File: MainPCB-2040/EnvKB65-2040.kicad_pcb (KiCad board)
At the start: 2 copper layers, 320.8 x 99.7 mm, 203 parts, among them J2 SKRKAEE020, J5 Conn_01x03_Male, U1 TLV73333PDBV, U3 RP2040, Y1 Crystal

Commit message: continued work on the RP2040 version
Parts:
- C1, C10, C4, D1, R3, R4, R5, R6, R8, U1: moved to B.Cu
- FLASH1: footprint Package_SO:SOIJ-8_5.3x5.3mm_P1.27mm -> Package_SON:SON-8-1EP_3x2mm_P0.5mm_EP1.4x1.6mm; moved to B.Cu
- moved R4 32.3 mm to (344.3, 106.0), turned to 270 degrees
- moved R5 29.3 mm to (365.5, 106.3)
- moved R8 27.3 mm to (340.4, 111.2)
- moved C10 26.7 mm to (343.3, 106.7), turned to 90 degrees
- moved R6 25.6 mm to (370.1, 106.4), turned to 180 degrees
- moved R3 25.3 mm to (345.2, 106.0), turned to 270 degrees
- moved FLASH1 23.1 mm to (349.1, 106.2), turned to 180 degrees
- moved D1 18.9 mm to (352.9, 100.9)
- moved U1 18.2 mm to (348.7, 99.8), turned to 180 degrees
- moved C1 14.3 mm to (352.7, 98.9)
- moved D3 7.73 mm to (342.0, 98.8)
- moved C4 6.40 mm to (344.6, 98.8), turned to 180 degrees
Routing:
- net USB_D-: track 0.00 -> 34.9 mm, vias 0 -> 2
- net USB_D+: track 0.00 -> 30.9 mm, vias 0 -> 2
- net VBUS: track 0.00 -> 23.5 mm, vias 0 -> 2
- net +3V3: track 0.00 -> 19.6 mm, vias 0 -> 2
- net Net-(D3-Pad2): track 0.00 -> 15.4 mm, vias 0 -> 1
- net GND: track 0.00 -> 12.8 mm, vias 4 -> 8
- net +1V1: track 0.00 -> 9.59 mm, vias 0 -> 5
- net VSYS: track 0.00 -> 6.70 mm
- net /QSPI_SS: track 0.00 -> 6.22 mm
- net /QSPI_SD1: track 0.00 -> 6.01 mm
- net /QSPI_SD2: track 0.00 -> 5.44 mm
- net /QSPI_SD3: track 0.00 -> 3.18 mm
- net /QSPI_SCLK: track 0.00 -> 2.49 mm
- net Net-(R3-Pad2): track 0.00 -> 1.97 mm
- net Net-(R4-Pad2): track 0.00 -> 1.96 mm
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- added copper zone on B.Cu, net +1V1
- added copper zone on B.Cu, net +3V3
- added copper zone on B.Cu, net VBUS

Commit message: finished off RP2040 version, needs general check overs and cleanup.
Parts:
- removed C17: 10uf 0402, Capacitor_SMD:C_0402_1005Metric
- removed C18: 100nf 0402, Capacitor_SMD:C_0402_1005Metric
- removed TP1, TP2, TP3, TP4, TP5, TP6, TP7, TP8: TestPoint, TestPoint:TestPoint_Pad_D1.0mm
- added J1: SKRKAEE020, Button_Switch_SMD:SW_Push_SPST_NO_Alps_SKRK, F.Cu at (357.3, 99.7)
- C11, C13, C19, C2, C5, R2, Y1: moved to B.Cu
- J5: footprint Connector_PinHeader_2.54mm:PinHeader_1x03_P2.54mm_Vertical -> Connector_PinHeader_1.00mm:PinHeader_1x03_P1.00mm_Horizontal
- moved Y1 49.9 mm to (346.7, 120.0), turned to 180 degrees
- moved C11 43.8 mm to (345.7, 117.2), turned to 270 degrees
- moved C19 43.4 mm to (346.4, 122.2)
- moved C15 37.8 mm to (346.5, 114.3)
- moved C2 37.5 mm to (349.5, 120.8), turned to 270 degrees
- moved J5 34.5 mm to (337.1, 101.0), turned to 90 degrees
- moved R2 32.3 mm to (351.1, 109.0)
- moved C7 31.7 mm to (345.8, 116.1)
- moved C16 31.0 mm to (346.2, 104.1), turned to 90 degrees
- moved C8 30.4 mm to (347.8, 109.2), turned to 180 degrees
- moved C14 25.6 mm to (348.9, 112.8)
- moved C13 25.1 mm to (340.3, 112.5), turned to 180 degrees
- moved J2 24.7 mm to (349.9, 99.7)
- moved C3 23.2 mm to (345.9, 109.2)
- moved C5 17.7 mm to (346.6, 105.2), turned to 45 degrees
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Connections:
- U3 pad 11: (no net) -> row2
- U3 pad 12: (no net) -> row1
- U3 pad 13: (no net) -> row0
- U3 pad 14: (no net) -> col14
- U3 pad 15: (no net) -> col13
- U3 pad 16: (no net) -> col12
- U3 pad 17: (no net) -> col11
- U3 pad 18: (no net) -> col10
- U3 pad 2: (no net) -> col15
- U3 pad 26: (no net) -> /RUN
- U3 pad 27: (no net) -> col9
- U3 pad 28: (no net) -> col8
- U3 pad 29: (no net) -> col7
- U3 pad 3: (no net) -> col16
- U3 pad 30: (no net) -> col6
- U3 pad 31: (no net) -> col5
- U3 pad 32: (no net) -> col4
- U3 pad 34: (no net) -> col3
- U3 pad 38: (no net) -> col2
- U3 pad 39: (no net) -> col1
- U3 pad 40: (no net) -> col0
- U3 pad 8: (no net) -> row4
- U3 pad 9: (no net) -> row3
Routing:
- net /RUN: track 0.00 -> 48.0 mm, vias 0 -> 1
- net GND: track 12.8 -> 41.6 mm, vias 8 -> 21
- net col13: track 113.9 -> 137.0 mm, vias 1 -> 3
- net /SWCLK: track 0.00 -> 21.6 mm, vias 0 -> 2
- net /SWD: track 0.00 -> 19.4 mm, vias 0 -> 2
- net VBUS: track 23.5 -> 5.10 mm
- net col4: track 278.7 -> 295.5 mm
- net col3: track 303.0 -> 319.3 mm
- net col12: track 144.2 -> 159.7 mm
- net col0: track 362.8 -> 378.1 mm
- net col2: track 297.0 -> 312.1 mm
- net col1: track 328.0 -> 342.9 mm
- net col11: track 161.3 -> 174.9 mm
- net col10: track 182.7 -> 194.5 mm
- net XOUT: track 0.00 -> 8.01 mm
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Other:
- board text added: "BOOTSEL"
- board text added: "GND"
- board text added: "RESET"
- board text added: "SWCLK"
- board text added: "SWD"
- board text removed: "http://github.com/Envious-Data/Env-KB65M"

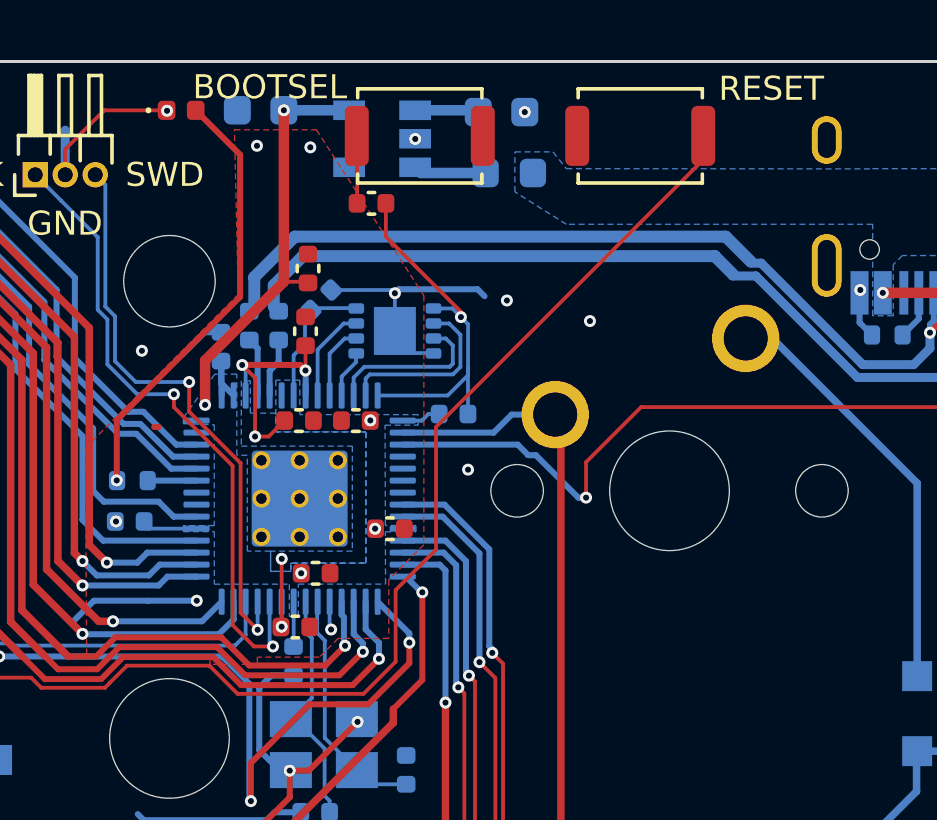
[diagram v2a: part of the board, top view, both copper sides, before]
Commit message: moved some resistors and capacitors to account for screw hole clearance for the stabilizer holes.
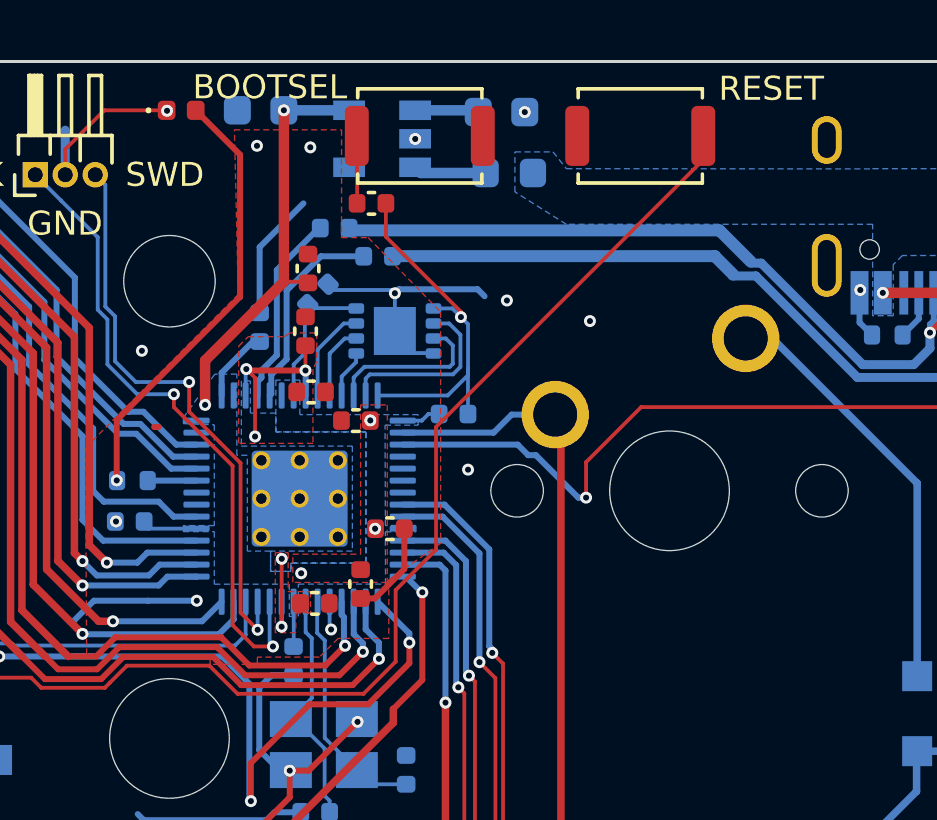
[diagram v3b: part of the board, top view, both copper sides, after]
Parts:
- moved R4 4.32 mm to (347.1, 102.8), turned to 180 degrees
- moved R3 4.04 mm to (348.5, 103.7), turned to 180 degrees
- moved C15 1.54 mm to (348.0, 114.6), turned to 270 degrees
- moved C10 1.44 mm to (344.6, 106.1)
- moved C3 1.04 mm to (346.3, 108.2)
- moved C7 1.02 mm to (346.4, 115.3)
- moved C5 0.22 mm to (346.5, 105.0)
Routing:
- net GND: track 41.6 -> 47.5 mm
- net USB_D+: track 32.1 -> 26.9 mm
- net Net-(R3-Pad2): track 1.97 -> 6.77 mm
- net USB_D-: track 31.0 -> 26.4 mm
- net Net-(R4-Pad2): track 1.96 -> 6.52 mm
- net +1V1: track 11.8 -> 10.0 mm
- added copper zone on F.Cu, net +1V1
- added copper zone on F.Cu, net +3V3
